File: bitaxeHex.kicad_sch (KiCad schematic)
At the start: 12 parts, among them J1 Conn_01x01, J2 Conn_01x01

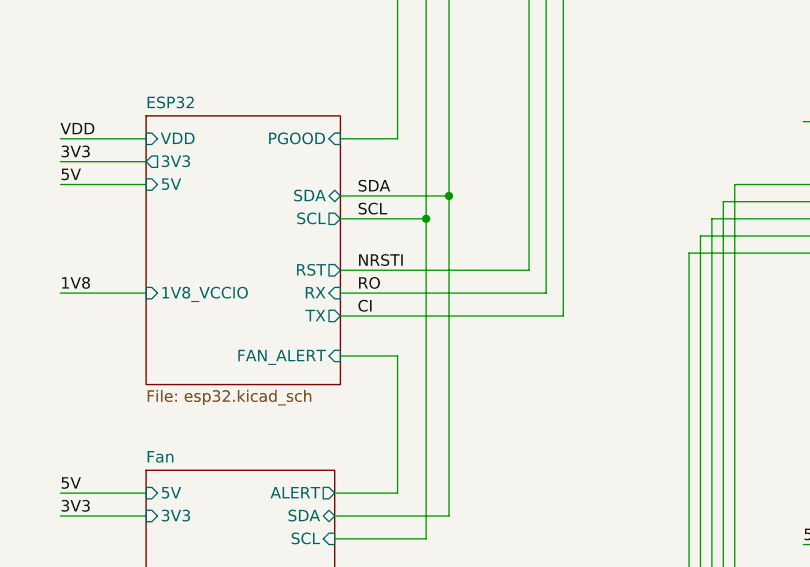
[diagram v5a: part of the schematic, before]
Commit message: add 10k pull-down on first BM1397 BI signal
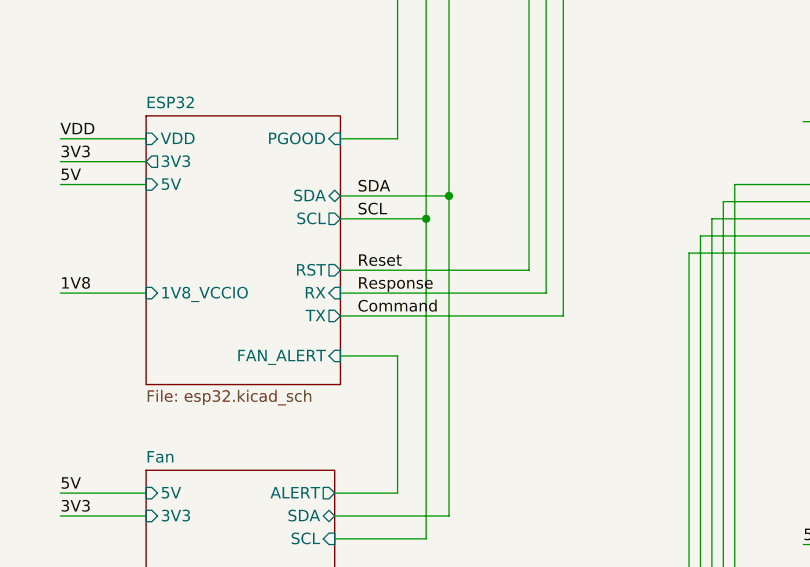
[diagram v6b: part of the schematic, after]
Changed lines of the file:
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@@
     (effects (font (size 1.27 1.27)) (justify left bottom))
   )
-  (label "CI" (at 94.615 90.805 0) (fields_autoplaced)
+  (label "Command" (at 94.615 90.805 0) (fields_autoplaced)
     (effects (font (size 1.27 1.27)) (justify left bottom))
   )
@@
     (effects (font (size 1.27 1.27)) (justify left bottom))
   )
-  (label "NRSTI" (at 94.615 85.725 0) (fields_autoplaced)
+  (label "Reset" (at 94.615 85.725 0) (fields_autoplaced)
     (effects (font (size 1.27 1.27)) (justify left bottom))
   )
@@
     (effects (font (size 1.27 1.27)) (justify left bottom))
   )
-  (label "RO" (at 94.615 88.265 0) (fields_autoplaced)
+  (label "Response" (at 94.615 88.265 0) (fields_autoplaced)
     (effects (font (size 1.27 1.27)) (justify left bottom))
   )
